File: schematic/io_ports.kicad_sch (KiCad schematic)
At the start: 5 parts, among them J1 Cartridge Port, J2 Expansion Port

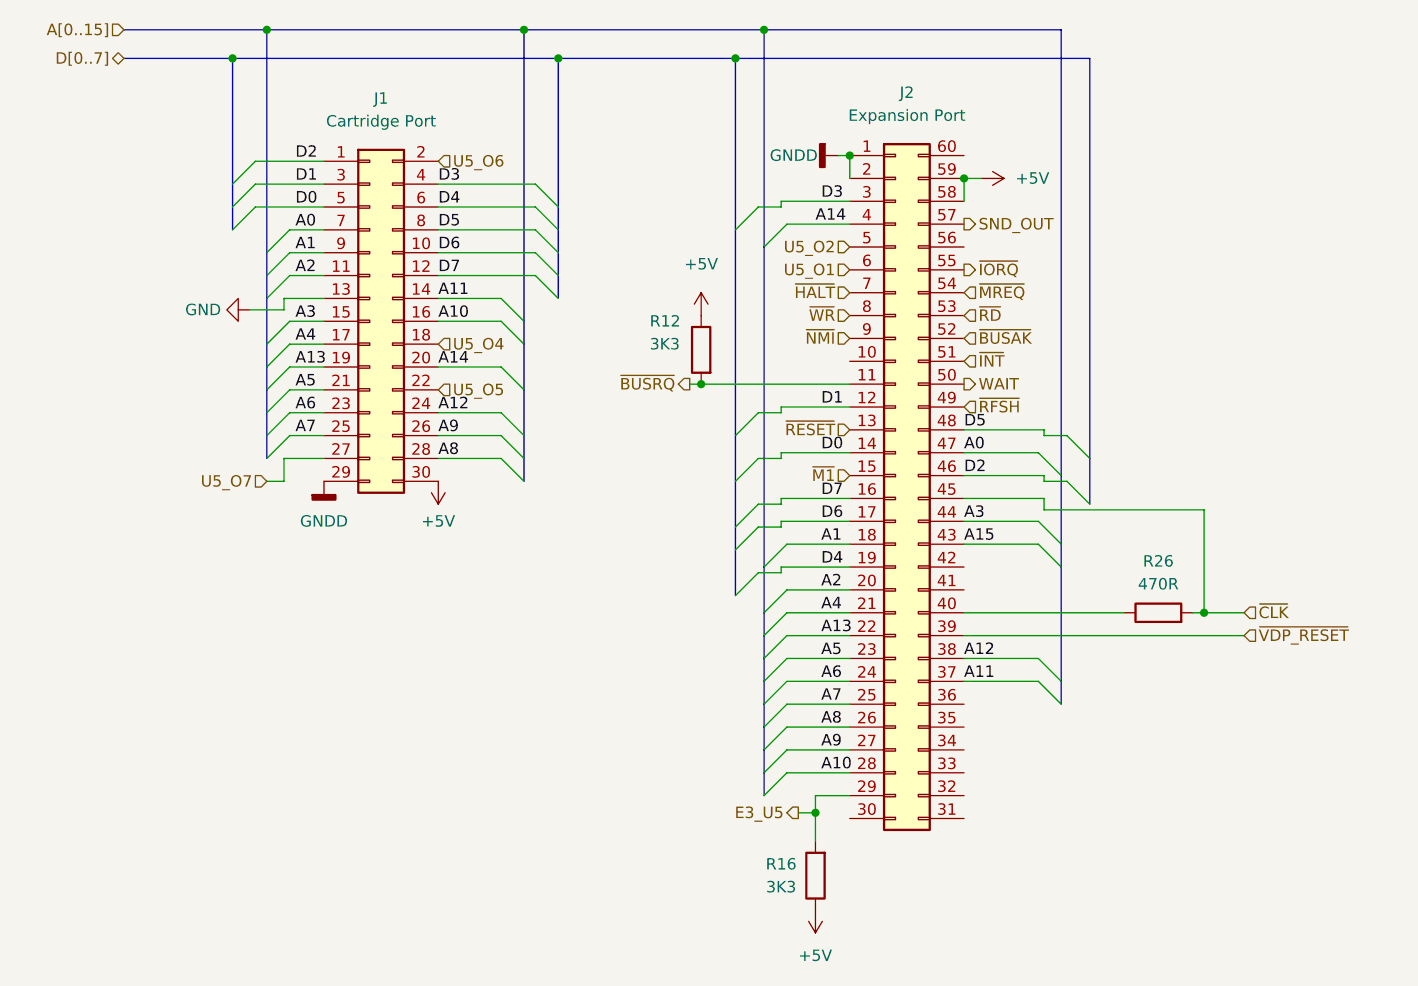
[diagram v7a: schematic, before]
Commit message: fixed some more line names, added a expansion port io pin.
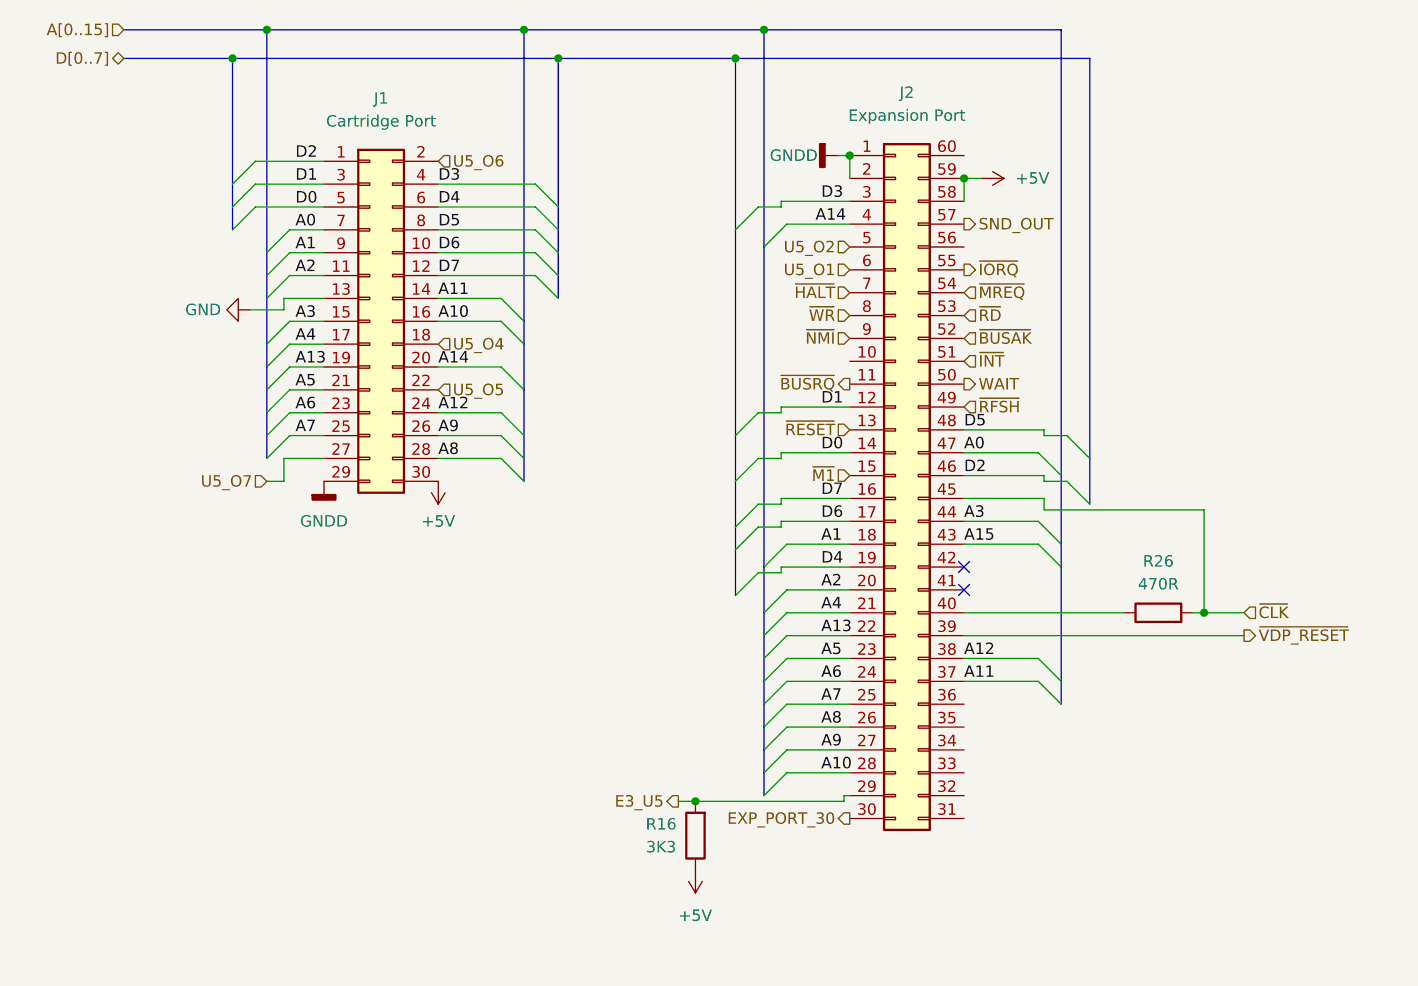
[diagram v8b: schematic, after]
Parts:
- removed R12: 3K3, symbol Device:R
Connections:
- net EXP_PORT_30: now reaches J2.30 (Pin_30)
- no-connect marks 0 -> 2
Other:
- moved on the sheet: R16
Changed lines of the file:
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@@
   (junction (at 153.67 33.02) (diameter 0) (color 0 0 0 0)
   )
-  (junction (at 146.685 72.39) (diameter 0) (color 0 0 0 0)
-  )
   (junction (at 94.615 36.195) (diameter 0) (color 0 0 0 0)
   )
   (junction (at 150.495 36.195) (diameter 0) (color 0 0 0 0)
   )
+  (junction (at 146.05 118.745) (diameter 0) (color 0 0 0 0)
+  )
   (junction (at 127 33.02) (diameter 0) (color 0 0 0 0)
   )
   (junction (at 163.195 46.99) (diameter 0) (color 0 0 0 0)
   )
-  (junction (at 159.385 120.015) (diameter 0) (color 0 0 0 0)
-  )
   (junction (at 130.81 36.195) (diameter 0) (color 0 0 0 0)
   )
   (junction (at 98.425 33.02) (diameter 0) (color 0 0 0 0)
   )
+  (no_connect (at 175.895 92.71))
+  (no_connect (at 175.895 95.25))
   (bus_entry (at 94.615 55.245) (size 2.54 -2.54)
     (stroke (width 0) (type default) (color 0 0 0 0))
@@
     (stroke (width 0) (type default) (color 0 0 0 0))
   )
-  (wire (pts (xy 146.685 72.39) (xy 163.195 72.39))
-    (stroke (width 0) (type default) (color 0 0 0 0))
-  )
   (wire (pts (xy 153.035 75.565) (xy 155.575 75.565))
     (stroke (width 0) (type default) (color 0 0 0 0))
@@
     (stroke (width 0) (type default) (color 0 0 0 0))
   )
+  (wire (pts (xy 162.56 118.11) (xy 162.56 118.745))
+    (stroke (width 0) (type default) (color 0 0 0 0))
+  )
   (bus (pts (xy 127 33.02) (xy 127 65.405))
     (stroke (width 0) (type default) (color 0 0 0 0))
@@
     (stroke (width 0) (type default) (color 0 0 0 0))
   )
-  (wire (pts (xy 145.415 72.39) (xy 146.685 72.39))
-    (stroke (width 0) (type default) (color 0 0 0 0))
-  )
   (bus (pts (xy 94.615 52.705) (xy 94.615 55.245))
     (stroke (width 0) (type default) (color 0 0 0 0))
@@
     (stroke (width 0) (type default) (color 0 0 0 0))
   )
-  (wire (pts (xy 159.385 118.11) (xy 163.195 118.11))
-    (stroke (width 0) (type default) (color 0 0 0 0))
-  )
   (wire (pts (xy 155.575 52.07) (xy 155.575 52.705))
     (stroke (width 0) (type default) (color 0 0 0 0))
@@
     (stroke (width 0) (type default) (color 0 0 0 0))
   )
+  (wire (pts (xy 163.195 118.11) (xy 162.56 118.11))
+    (stroke (width 0) (type default) (color 0 0 0 0))
+  )
   (wire (pts (xy 175.895 97.79) (xy 193.675 97.79))
     (stroke (width 0) (type default) (color 0 0 0 0))
@@
     (stroke (width 0) (type default) (color 0 0 0 0))
   )
-  (wire (pts (xy 159.385 120.015) (xy 159.385 123.19))
-    (stroke (width 0) (type default) (color 0 0 0 0))
-  )
   (wire (pts (xy 100.33 64.135) (xy 96.52 64.135))
     (stroke (width 0) (type default) (color 0 0 0 0))
@@
     (stroke (width 0) (type default) (color 0 0 0 0))
   )
-  (wire (pts (xy 157.48 120.015) (xy 159.385 120.015))
-    (stroke (width 0) (type default) (color 0 0 0 0))
-  )
   (bus (pts (xy 150.495 55.245) (xy 150.495 78.105))
     (stroke (width 0) (type default) (color 0 0 0 0))
@@
     (stroke (width 0) (type default) (color 0 0 0 0))
   )
-  (wire (pts (xy 159.385 118.11) (xy 159.385 120.015))
-    (stroke (width 0) (type default) (color 0 0 0 0))
-  )
   (wire (pts (xy 184.785 86.36) (xy 202.565 86.36))
     (stroke (width 0) (type default) (color 0 0 0 0))
@@
     (stroke (width 0) (type default) (color 0 0 0 0))
   )
+  (wire (pts (xy 146.05 118.745) (xy 162.56 118.745))
+    (stroke (width 0) (type default) (color 0 0 0 0))
+  )
   (bus (pts (xy 130.81 36.195) (xy 150.495 36.195))
     (stroke (width 0) (type default) (color 0 0 0 0))
@@
     (stroke (width 0) (type default) (color 0 0 0 0))
   )
+  (wire (pts (xy 144.145 118.745) (xy 146.05 118.745))
+    (stroke (width 0) (type default) (color 0 0 0 0))
+  )
   (bus (pts (xy 98.425 78.105) (xy 98.425 80.645))
     (stroke (width 0) (type default) (color 0 0 0 0))
@@
     (effects (font (size 1.27 1.27)) (justify left bottom))
   )
+  (hierarchical_label "EXP_PORT_30" (shape output) (at 163.195 120.65 180)
+    (effects (font (size 1.27 1.27)) (justify right))
+  )
   (hierarchical_label "WAIT" (shape output) (at 175.895 72.39 0)
     (effects (font (size 1.27 1.27)) (justify left))
@@
     (effects (font (size 1.27 1.27)) (justify right))
   )
-  (hierarchical_label "~{BUSRQ}" (shape output) (at 145.415 72.39 180)
+  (hierarchical_label "~{BUSRQ}" (shape output) (at 163.195 72.39 180)
     (effects (font (size 1.27 1.27)) (justify right))
   )
@@
     (effects (font (size 1.27 1.27)) (justify right))
   )
-  (hierarchical_label "E3_U5" (shape output) (at 157.48 120.015 180)
-    (effects (font (size 1.27 1.27)) (justify right))
-  )
-  (hierarchical_label "~{VDP_RESET}" (shape input) (at 207.01 100.33 0)
+  (hierarchical_label "E3_U5" (shape output) (at 144.145 118.745 180)
+    (effects (font (size 1.27 1.27)) (justify right))
+  )
+  (hierarchical_label "~{VDP_RESET}" (shape output) (at 207.01 100.33 0)
     (effects (font (size 1.27 1.27)) (justify left))
   )
@@
     (pin "9")
   )
-  (symbol (lib_id "power:+5V") (at 159.385 130.81 180) (unit 1)
+  (symbol (lib_id "power:+5V") (at 146.05 126.365 180) (unit 1)
     (in_bom yes) (on_board yes)
-    (property "Reference" "#PWR?" (id 0) (at 159.385 127 0)
-      (effects (font (size 1.27 1.27)) hide)
-    )
-    (property "Value" "+5V" (id 1) (at 157.48 135.89 0)
+    (property "Reference" "#PWR?" (id 0) (at 146.05 122.555 0)
+      (effects (font (size 1.27 1.27)) hide)
+    )
+    (property "Value" "+5V" (id 1) (at 144.145 131.445 0)
       (effects (font (size 1.27 1.27)) (justify right))
     )
-    (property "Footprint" "" (id 2) (at 159.385 130.81 0)
-      (effects (font (size 1.27 1.27)) hide)
-    )
-    (property "Datasheet" "" (id 3) (at 159.385 130.81 0)
+    (property "Footprint" "" (id 2) (at 146.05 126.365 0)
+      (effects (font (size 1.27 1.27)) hide)
+    )
+    (property "Datasheet" "" (id 3) (at 146.05 126.365 0)
       (effects (font (size 1.27 1.27)) hide)
     )
@@
     (pin "9")
   )
-  (symbol (lib_id "Device:R") (at 159.385 127 180) (unit 1)
+  (symbol (lib_id "Device:R") (at 146.05 122.555 180) (unit 1)
     (in_bom yes) (on_board yes)
-    (property "Reference" "R16" (id 0) (at 155.575 125.73 0))
-    (property "Value" "3K3" (id 1) (at 155.575 128.27 0))
-    (property "Footprint" "" (id 2) (at 161.163 127 90)
-      (effects (font (size 1.27 1.27)) hide)
-    )
-    (property "Datasheet" "~" (id 3) (at 159.385 127 0)
-      (effects (font (size 1.27 1.27)) hide)
-    )
-    (pin "1")
-    (pin "2")
-  )
-  (symbol (lib_id "power:+5V") (at 146.685 64.77 0) (unit 1)
-    (in_bom yes) (on_board yes) (fields_autoplaced)
-    (property "Reference" "#PWR?" (id 0) (at 146.685 68.58 0)
-      (effects (font (size 1.27 1.27)) hide)
-    )
-    (property "Value" "+5V" (id 1) (at 146.685 59.055 0))
-    (property "Footprint" "" (id 2) (at 146.685 64.77 0)
-      (effects (font (size 1.27 1.27)) hide)
-    )
-    (property "Datasheet" "" (id 3) (at 146.685 64.77 0)
-      (effects (font (size 1.27 1.27)) hide)
-    )
-    (pin "1")
-  )
-  (symbol (lib_id "Device:R") (at 146.685 68.58 0) (mirror y) (unit 1)
-    (in_bom yes) (on_board yes)
-    (property "Reference" "R12" (id 0) (at 140.97 65.405 0)
-      (effects (font (size 1.27 1.27)) (justify right))
-    )
-    (property "Value" "3K3" (id 1) (at 140.97 67.945 0)
-      (effects (font (size 1.27 1.27)) (justify right))
-    )
-    (property "Footprint" "" (id 2) (at 148.463 68.58 90)
-      (effects (font (size 1.27 1.27)) hide)
-    )
-    (property "Datasheet" "~" (id 3) (at 146.685 68.58 0)
-      (effects (font (size 1.27 1.27)) hide)
-    )
+    (property "Reference" "R16" (id 0) (at 142.24 121.285 0))
+    (property "Value" "3K3" (id 1) (at 142.24 123.825 0))
+    (property "Footprint" "" (id 2) (at 147.828 122.555 90)
+      (effects (font (size 1.27 1.27)) hide)
+    )
+    (property "Datasheet" "~" (id 3) (at 146.05 122.555 0)
+      (effects (font (size 1.27 1.27)) hide)
+    )
